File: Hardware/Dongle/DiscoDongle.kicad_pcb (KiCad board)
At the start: 2 copper layers, 60.5 x 18.8 mm, 22 parts, among them J1 RJ45, P1 USB_B, P2 FTDI, U1 FT232RL, U2 ISL81487E

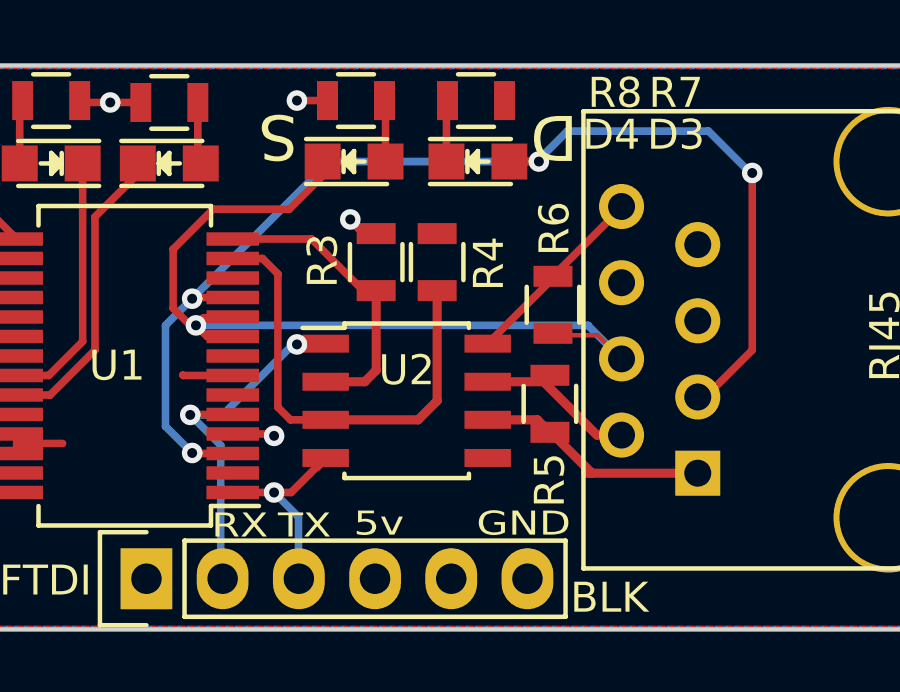
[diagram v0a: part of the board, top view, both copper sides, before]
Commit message: Update the DiscoDongle with more LEDs and pull-up on daisy line.
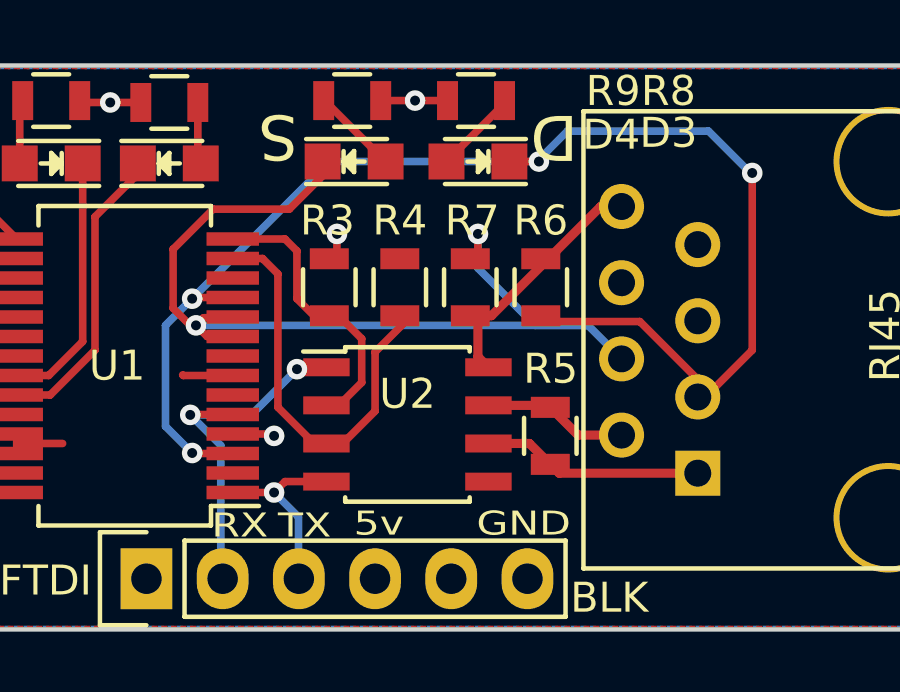
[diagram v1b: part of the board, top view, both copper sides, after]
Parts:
- added R9: 200, Resistors_SMD:R_0805, F.Cu at (74.0, 35.3)
- R7: value 200 -> 20k
- moved R7 6.23 mm to (77.9, 41.5), turned to 90 degrees
- moved R8 4.00 mm to (78.1, 35.3)
- moved R3 1.77 mm to (73.2, 41.5)
- moved R4 1.50 mm to (75.6, 41.5)
- moved R5 1.07 mm to (80.6, 46.5)
- moved U2 0.79 mm to (75.8, 46.1)
- moved R6 0.71 mm to (80.3, 41.5)
- turned D3 to 180 degrees
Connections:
- D3 pad 1: Net-(D3-Pad1) -> Daisy
- D3 pad 2: Daisy -> Net-(D3-Pad2)
- R6 pad 2: Signal -> Daisy
- R7 pad 1: GND -> +5V
- R7 pad 2: Net-(D3-Pad1) -> Signal
- R8 pad 2: Net-(D4-Pad2) -> Net-(D3-Pad2)
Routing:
- net Daisy: track 39.6 -> 47.0 mm
- net Signal: track 29.4 -> 33.2 mm, vias 1 -> 2
- net +5V: track 23.7 -> 27.5 mm
- net Net-(D3-Pad2): track 0.00 -> 3.06 mm
- net Net-(D3-Pad1): track 2.05 -> 0.00 mm
- net Net-(R4-Pad1): track 15.6 -> 14.0 mm
- net Net-(D4-Pad2): track 2.05 -> 3.21 mm
- net Net-(P2-Pad3): track 7.21 -> 6.50 mm
- net Net-(R3-Pad2): track 10.2 -> 9.56 mm
- net Net-(J1-Pad1): track 7.96 -> 7.39 mm

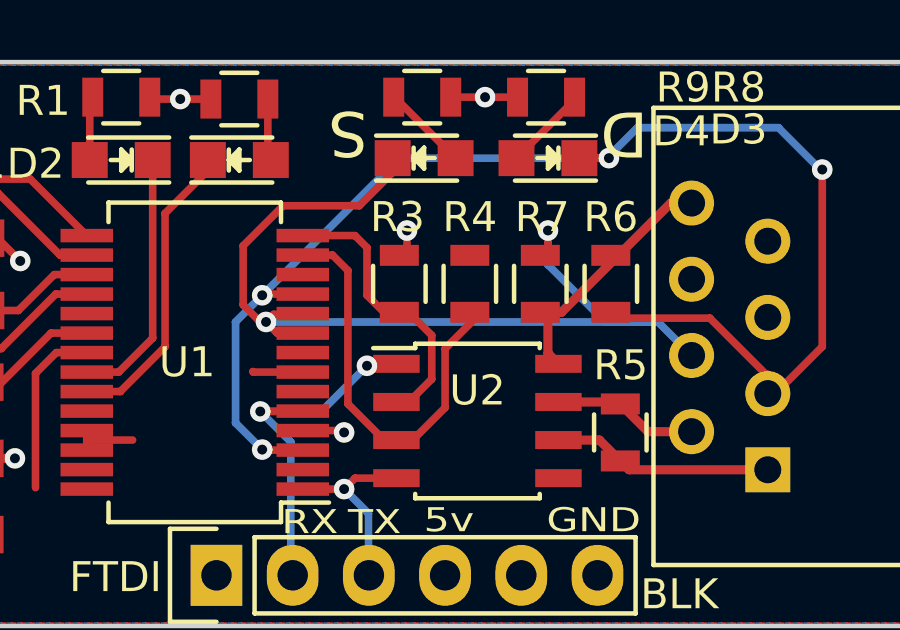
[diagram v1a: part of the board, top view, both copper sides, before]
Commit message: Tie the RE and DE together on the TXEN line of FTDI
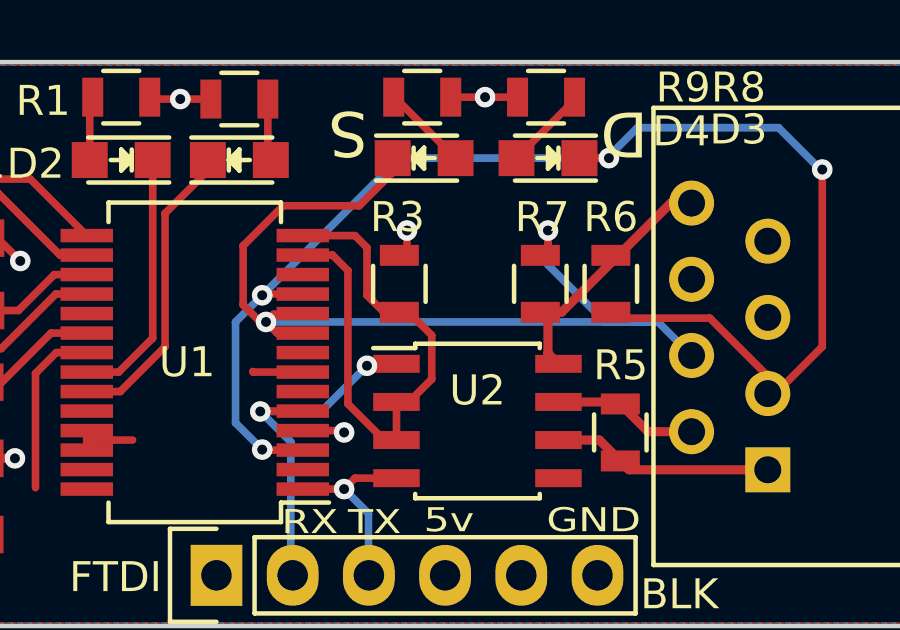
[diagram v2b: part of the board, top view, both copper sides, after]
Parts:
- removed R4: 20k, Resistors_SMD:R_0805
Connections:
- U1 pad 14: Net-(R3-Pad2) -> Net-(U1-Pad14)
- U2 pad 2: Net-(R3-Pad2) -> Net-(R4-Pad1)
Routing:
- net Net-(R3-Pad2): track 9.56 -> 5.76 mm
- net Net-(R4-Pad1): track 14.0 -> 11.6 mm
- net Net-(U1-Pad14): track 0.00 -> 2.31 mm
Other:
- board text added: "2016 - rev3"
- board text removed: "2016"
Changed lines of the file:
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@@
 (kicad_pcb (version 4) (host pcbnew 4.0.2-stable)
   (general
-    (links 63)
+    (links 60)
     (no_connects 0)
     (area 37.912599 32.1286 99.947801 53.171901)
     (thickness 1.6)
     (drawings 13)
-    (tracks 173)
+    (tracks 170)
     (zones 0)
-    (modules 23)
-    (nets 30)
+    (modules 22)
+    (nets 31)
   )
   (page User 150.012 105.004)
@@
     (34 B.Paste user)
     (35 F.Paste user)
-    (36 B.SilkS user hide)
+    (36 B.SilkS user)
     (37 F.SilkS user)
     (38 B.Mask user)
@@
   (net 28 "Net-(U1-Pad2)")
   (net 29 "Net-(D3-Pad2)")
+  (net 30 "Net-(U1-Pad14)")
   (net_class Default "This is the default net class."
     (clearance 0.1524)
@@
     (add_net "Net-(R4-Pad1)")
     (add_net "Net-(U1-Pad12)")
+    (add_net "Net-(U1-Pad14)")
     (add_net "Net-(U1-Pad19)")
     (add_net "Net-(U1-Pad2)")
@@
   )
   (module Resistors_SMD:R_0805 (layer F.Cu)
-    (at 75.565 41.529 90)
-    (descr "Resistor SMD 0805, reflow soldering, Vishay (see dcrcw.pdf)")
-    (tags "resistor 0805")
-    (attr smd)
-    (fp_text reference R4 (at 2.2225 0 180) (layer F.SilkS)
-      (effects (font (size 1 1) (thickness 0.15)))
-    )
-    (fp_text value 20k (at 0 2.1 90) (layer F.Fab) hide
-      (effects (font (size 1 1) (thickness 0.15)))
-    )
-    (fp_line (start -1.6 -1) (end 1.6 -1) (layer F.CrtYd) (width 0.05))
-    (fp_line (start -1.6 1) (end 1.6 1) (layer F.CrtYd) (width 0.05))
-    (fp_line (start -1.6 -1) (end -1.6 1) (layer F.CrtYd) (width 0.05))
-    (fp_line (start 1.6 -1) (end 1.6 1) (layer F.CrtYd) (width 0.05))
-    (fp_line (start 0.6 0.875) (end -0.6 0.875) (layer F.SilkS) (width 0.15))
-    (fp_line (start -0.6 -0.875) (end 0.6 -0.875) (layer F.SilkS) (width 0.15))
-    (pad 1 smd rect (at -0.95 0 90) (size 0.7 1.3) (layers F.Cu F.Paste F.Mask)
-      (net 18 "Net-(R4-Pad1)"))
-    (pad 2 smd rect (at 0.95 0 90) (size 0.7 1.3) (layers F.Cu F.Paste F.Mask)
-      (net 26 GND))
-    (model Resistors_SMD.3dshapes/R_0805.wrl
-      (at (xyz 0 0 0))
-      (scale (xyz 1 1 1))
-      (rotate (xyz 0 0 0))
-    )
-  )
-  (module Resistors_SMD:R_0805 (layer F.Cu)
     (at 80.5815 46.482 270)
     (descr "Resistor SMD 0805, reflow soldering, Vishay (see dcrcw.pdf)")
@@
       (net 18 "Net-(R4-Pad1)"))
     (pad 14 smd rect (at -3.6 4.225 180) (size 1.75 0.45) (layers F.Cu F.Paste F.Mask)
-      (net 17 "Net-(R3-Pad2)"))
+      (net 30 "Net-(U1-Pad14)"))
     (pad 15 smd rect (at 3.6 4.225 180) (size 1.75 0.45) (layers F.Cu F.Paste F.Mask)
       (net 12 "Net-(P1-Pad3)"))
@@
       (net 14 "Net-(P2-Pad2)"))
     (pad 2 smd rect (at -2.7 -0.635) (size 1.55 0.6) (layers F.Cu F.Paste F.Mask)
-      (net 17 "Net-(R3-Pad2)"))
+      (net 18 "Net-(R4-Pad1)"))
     (pad 3 smd rect (at -2.7 0.635) (size 1.55 0.6) (layers F.Cu F.Paste F.Mask)
       (net 18 "Net-(R4-Pad1)"))
@@
     (effects (font (size 1.5 1.5) (thickness 0.2)))
   )
-  (gr_text 2016 (at 75.6412 45.9232) (layer B.SilkS)
-    (effects (font (size 1.5 1.5) (thickness 0.2)) (justify mirror))
+  (gr_text "2016 - rev3" (at 78.5495 45.466) (layer B.SilkS)
+    (effects (font (size 1.2 1.2) (thickness 0.2)) (justify left mirror))
   )
   (gr_text DiscoDongle2 (at 68.7324 42.8752) (layer B.SilkS)
@@
   (segment (start 72.1868 49.183) (end 72.1868 51.2572) (width 0.254) (layer B.Cu) (net 15))
   (segment (start 69.9956 48.3702) (end 71.374 48.3702) (width 0.254) (layer F.Cu) (net 15))
-  (segment (start 73.533 45.466) (end 73.119 45.466) (width 0.254) (layer F.Cu) (net 17))
-  (segment (start 74.295 44.704) (end 73.533 45.466) (width 0.254) (layer F.Cu) (net 17))
-  (segment (start 74.295 43.2435) (end 74.295 44.704) (width 0.254) (layer F.Cu) (net 17))
   (segment (start 73.5305 42.479) (end 74.295 43.2435) (width 0.254) (layer F.Cu) (net 17))
   (segment (start 73.4695 42.479) (end 73.5305 42.479) (width 0.254) (layer F.Cu) (net 17))
   (segment (start 73.4695 42.479) (end 72.705 42.479) (width 0.254) (layer F.Cu) (net 17))
-  (segment (start 71.7362 39.9202) (end 69.9956 39.9202) (width 0.254) (layer F.Cu) (net 17))
-  (segment (start 72.136 40.32) (end 71.7362 39.9202) (width 0.254) (layer F.Cu) (net 17))
+  (segment (start 72.705 42.479) (end 72.136 41.91) (width 0.254) (layer F.Cu) (net 17))
+  (segment (start 74.295 43.2435) (end 74.295 44.704) (width 0.254) (layer F.Cu) (net 17))
   (segment (start 72.136 41.91) (end 72.136 40.32) (width 0.254) (layer F.Cu) (net 17))
-  (segment (start 72.705 42.479) (end 72.136 41.91) (width 0.254) (layer F.Cu) (net 17))
-  (segment (start 75.946 42.479) (end 75.946 42.4815) (width 0.254) (layer F.Cu) (net 18))
-  (segment (start 75.946 42.4815) (end 74.7395 43.688) (width 0.254) (layer F.Cu) (net 18))
-  (segment (start 74.7395 43.688) (end 74.7395 45.6565) (width 0.254) (layer F.Cu) (net 18))
-  (segment (start 74.7395 45.6565) (end 73.66 46.736) (width 0.254) (layer F.Cu) (net 18))
+  (segment (start 73.119 45.466) (end 73.119 46.736) (width 0.254) (layer F.Cu) (net 18) (status C00000))
+  (segment (start 73.533 45.466) (end 73.119 45.466) (width 0.254) (layer F.Cu) (net 18))
+  (segment (start 74.295 44.704) (end 73.533 45.466) (width 0.254) (layer F.Cu) (net 18))
   (segment (start 73.66 46.736) (end 73.119 46.736) (width 0.254) (layer F.Cu) (net 18))
   (segment (start 73.119 46.736) (end 72.7075 46.736) (width 0.254) (layer F.Cu) (net 18))
@@
   (segment (start 79.055 35.40248) (end 77.11948 37.338) (width 0.254) (layer F.Cu) (net 29))
   (segment (start 79.21752 35.46852) (end 79.055 35.306) (width 0.254) (layer F.Cu) (net 29))
+  (segment (start 71.7362 39.9202) (end 69.9956 39.9202) (width 0.254) (layer F.Cu) (net 30))
+  (segment (start 72.136 40.32) (end 71.7362 39.9202) (width 0.254) (layer F.Cu) (net 30))
   (zone (net 26) (net_name GND) (layer F.Cu) (hatch edge 0.508)
     (connect_pads (clearance 0.508))

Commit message: Update pours
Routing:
- net Net-(U1-Pad14): track 2.31 -> 1.74 mm
- net Net-(R3-Pad2): track 5.76 -> 6.33 mm
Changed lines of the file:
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@@
   )
   (setup
-    (last_trace_width 0.254)
+    (last_trace_width 0.1524)
     (user_trace_width 0.254)
     (user_trace_width 0.305)
@@
   (segment (start 74.295 43.2435) (end 74.295 44.704) (width 0.254) (layer F.Cu) (net 17))
   (segment (start 72.136 41.91) (end 72.136 40.32) (width 0.254) (layer F.Cu) (net 17))
-  (segment (start 73.119 45.466) (end 73.119 46.736) (width 0.254) (layer F.Cu) (net 18) (status C00000))
+  (segment (start 72.136 40.32) (end 71.7362 39.9202) (width 0.254) (layer F.Cu) (net 17))
+  (segment (start 73.119 45.466) (end 73.119 46.736) (width 0.254) (layer F.Cu) (net 18))
   (segment (start 73.533 45.466) (end 73.119 45.466) (width 0.254) (layer F.Cu) (net 18))
   (segment (start 74.295 44.704) (end 73.533 45.466) (width 0.254) (layer F.Cu) (net 18))
@@
   (segment (start 79.21752 35.46852) (end 79.055 35.306) (width 0.254) (layer F.Cu) (net 29))
   (segment (start 71.7362 39.9202) (end 69.9956 39.9202) (width 0.254) (layer F.Cu) (net 30))
-  (segment (start 72.136 40.32) (end 71.7362 39.9202) (width 0.254) (layer F.Cu) (net 30))
   (zone (net 26) (net_name GND) (layer F.Cu) (hatch edge 0.508)
     (connect_pads (clearance 0.508))

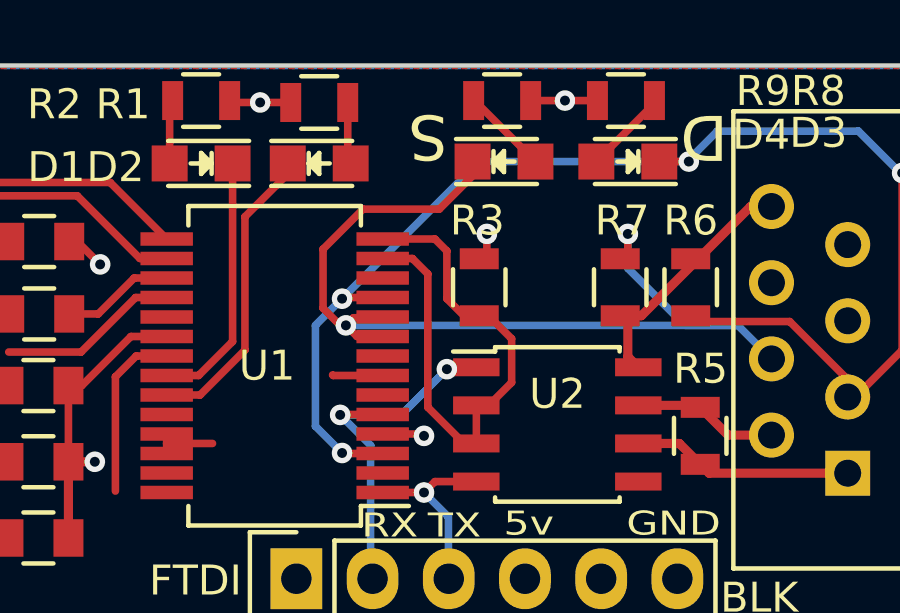
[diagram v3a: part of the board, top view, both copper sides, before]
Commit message: Fix wiring to TXEN and pull-down resistor
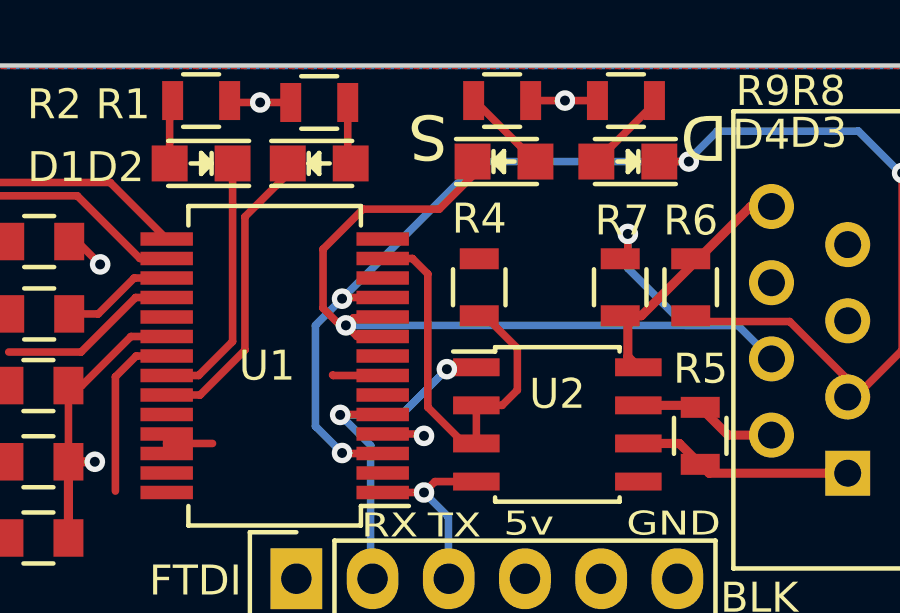
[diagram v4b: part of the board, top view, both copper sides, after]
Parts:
- removed R3: 20k, Resistors_SMD:R_0805
- added R4: 20k, Resistors_SMD:R_0805, F.Cu at (73.2, 41.5)
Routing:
- net Net-(R3-Pad2): track 6.33 -> 0.00 mm
- net Net-(R4-Pad1): track 11.6 -> 16.0 mm
- net Net-(U1-Pad14): track 1.74 -> 0.00 mm
- net +5V: track 27.5 -> 26.7 mm, vias 6 -> 5
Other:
- board text added: "2016 - rev4"
- board text removed: "2016 - rev3"
